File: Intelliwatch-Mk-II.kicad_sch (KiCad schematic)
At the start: 72 parts, among them J1 USB_C_Receptacle_USB2.0_16P, J101 DC Power Input, J2 CONN LCD 1.8 TFT SPI, J3 Conn 7S-4D HW-069 I2C, J4 Flashlight Terminals, J5 Voltmeter Probes, J6 DC Power Input, Q2 NDS331N, SW1 EN Button, SW2 PROG Button, SW3 Cherry MX Keyswitch, SW4 Cherry MX Keyswitch, SW5 Cherry MX Keyswitch, SW6 Cherry MX Keyswitch, SW7 LCD LED SPST, SW8 PWR SPST, SW9 PWR SPST, U1 LM7805, U10 SY8120IABC, U2 CH340C, U3 SN74HC02N, U4 LM1117T-3.3, U5 74AHC1G04GW_125, U6 74AHC1G04GW_125, U7 ESP32-WROOM-32UE, U8 QMC5883L, U9 MCP3421A0T-ECH

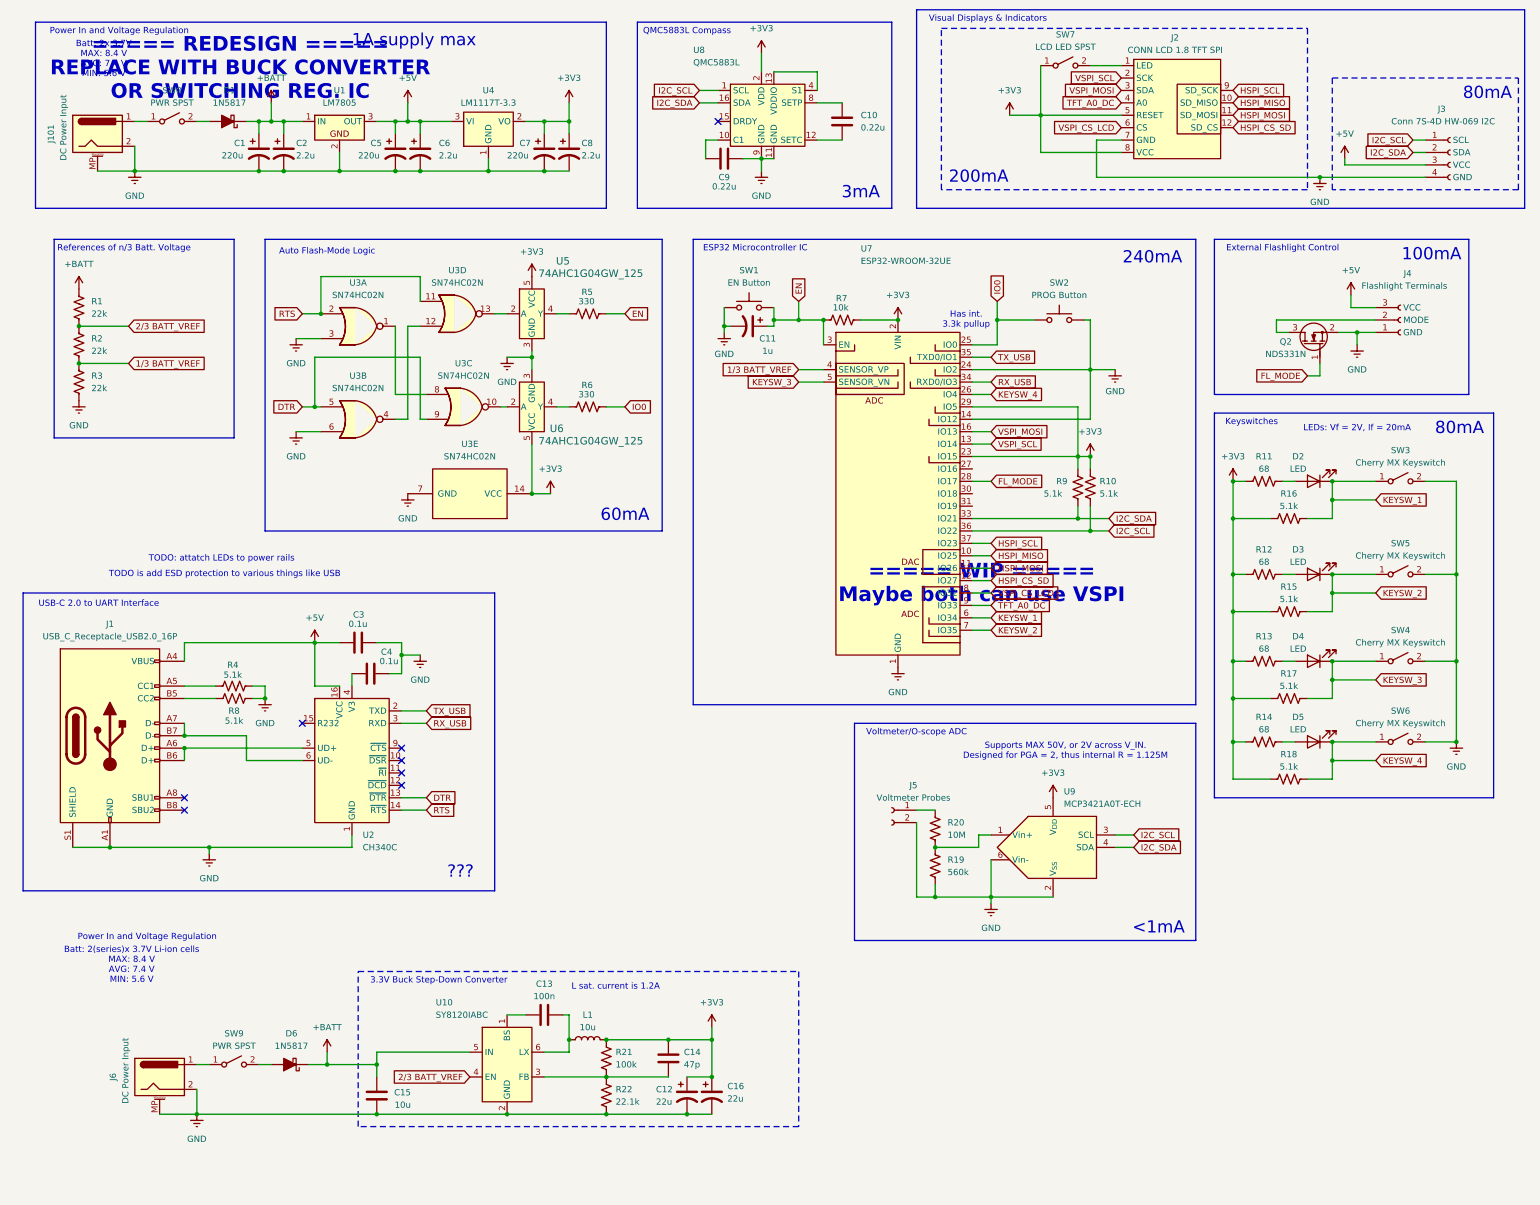
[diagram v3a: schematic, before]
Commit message: ADDED ESD protection diodes. FIXED power supply and voltage regulation. WIP figuring out if shared SPI bus is possible.
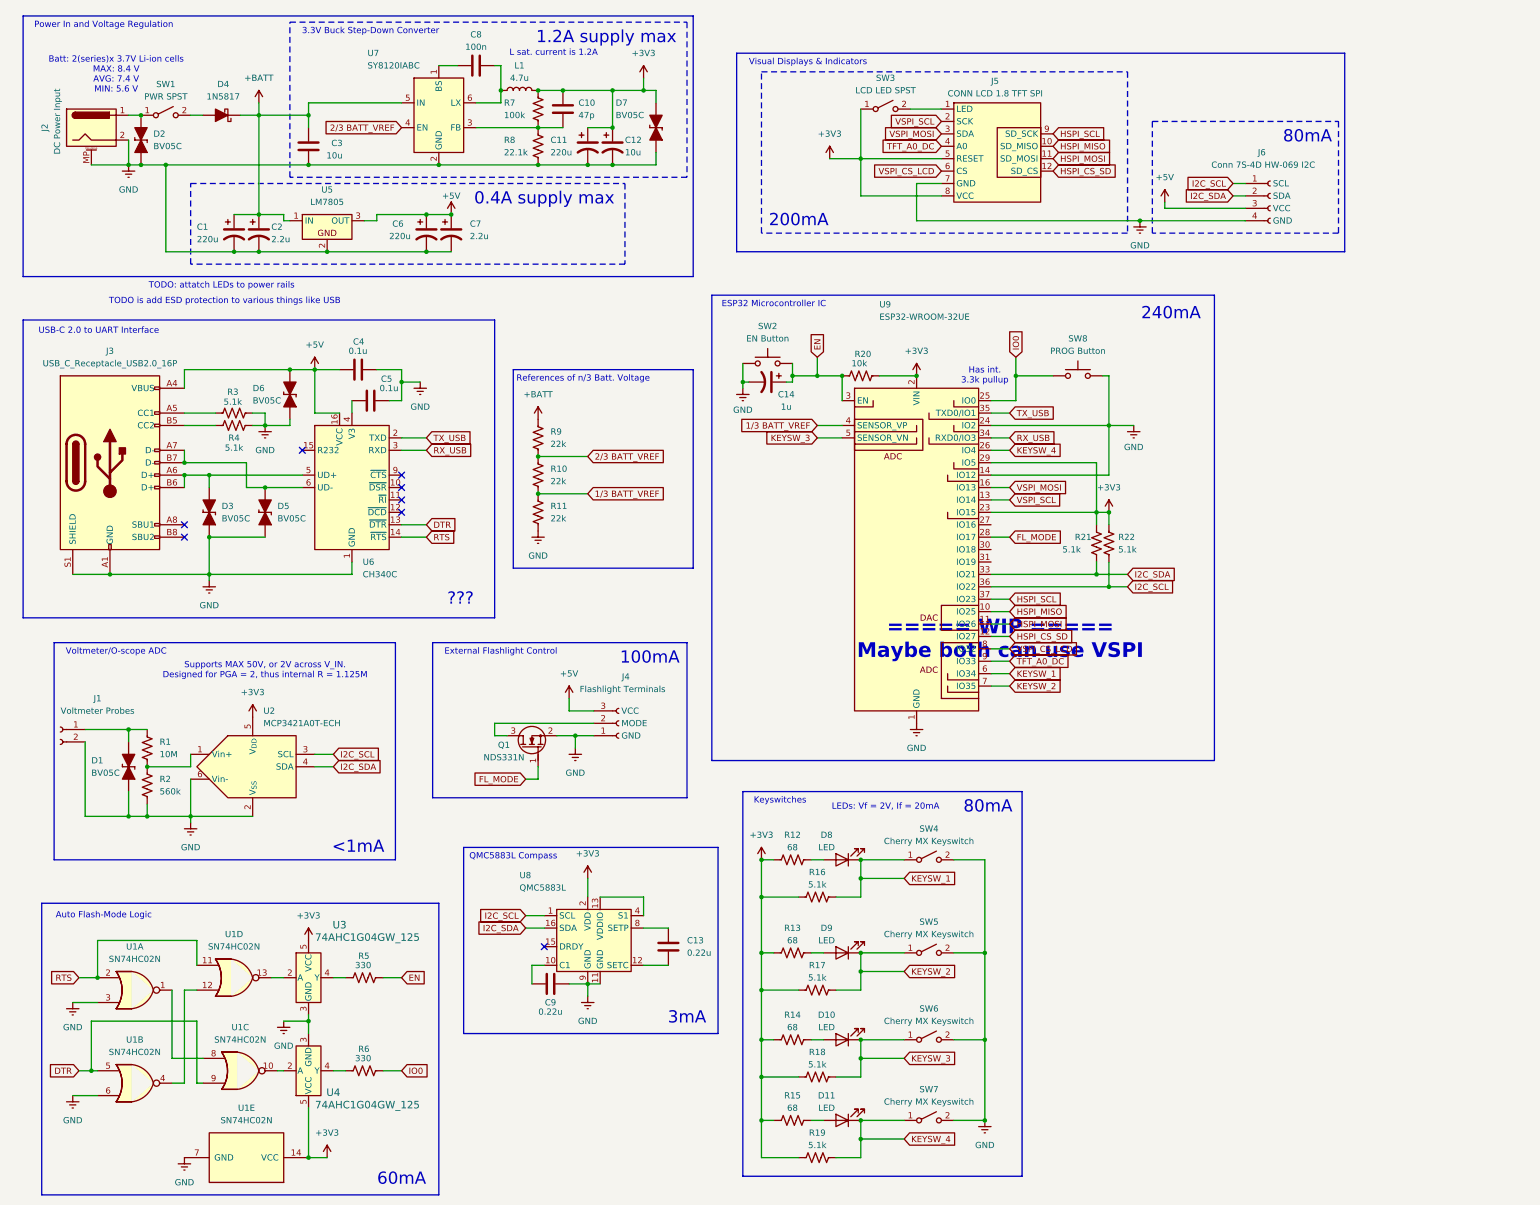
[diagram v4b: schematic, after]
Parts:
- removed C5: 220u, symbol Device:C_Polarized_US
- removed C8: 2.2u, symbol Device:C_Polarized_US
- removed D1: 1N5817, symbol Device:D_Schottky_Filled
- removed J101: DC Power Input, Connector_BarrelJack:BarrelJack_Horizontal, symbol Connector:Barrel_Jack_MountingPin
- removed SW8: PWR SPST, symbol Switch:SW_SPST
- removed U1: LM7805, PCM_Package_TO_SOT_THT_AKL:TO-220-3_Vertical, symbol PCM_Voltage_Regulator_AKL:LM7805CT
- removed U4: LM1117T-3.3, PCM_Package_TO_SOT_THT_AKL:TO-220-3_Vertical, symbol Regulator_Linear:LM1117T-3.3
- added D1, D2, D3, D5, D6, D7: BV05C, PCM_Diode_SMD_AKL:D_SOD-323_TVS, symbol PCM_Diode_TVS_AKL:D_TVS_Bidirectional_Generic
- added U5: LM7805, PCM_Package_TO_SOT_THT_AKL:TO-220-3_Vertical, symbol PCM_Voltage_Regulator_AKL:LM7805CT
- C11: renamed from C12; value 22u -> 220u
- C12: renamed from C16; value 22u -> 10u
- C6: value 2.2u -> 220u
- C7: value 220u -> 2.2u
- J1: renamed from J5; footprint (none) -> ZCustomFootprints:Standard IO Holes
- L1: value 10u -> 4.7u
- renumbered C14 to C10, C10 to C13, C11 to C14, C15 to C3, C3 to C4, C4 to C5, C13 to C8, D4 to D10, D5 to D11, D6 to D4, D2 to D8, D3 to D9, J6 to J2, J1 to J3, J2 to J5, J3 to J6, Q2 to Q1, R20 to R1, R2 to R10, R3 to R11, R11 to R12, R12 to R13, R13 to R14, R14 to R15, R15 to R17, R17 to R18, R18 to R19, R19 to R2, R7 to R20, R9 to R21, R10 to R22, R4 to R3, R8 to R4, R21 to R7, R22 to R8, R1 to R9, SW9 to SW1, SW1 to SW2, SW7 to SW3, SW3 to SW4, SW4 to SW6, SW6 to SW7, SW2 to SW8, U3 to U1, U9 to U2, U5 to U3, U6 to U4, U2 to U6, U10 to U7, U7 to U9
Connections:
- net +3V3: now also D7.1 (K); no longer C7.1
- net +5V: now also C7.1, D6.1 (K), U5.3 (OUT)
- net +BATT: now also U5.1 (IN)
- net GND: now also D1.2 (A), D2.2 (A), D3.2 (A), D5.2 (A), D6.2 (A), D7.2 (A), U5.2
- net at J2.1, SW1.1 (A): now also D2.1 (K)
- net at J1.1 (Pin_1), R1.2: now also D1.1 (K)
- net at J3.A6 (D+), J3.B6 (D+), U6.5 (UD+): now also D3.1 (K)
- net at J3.A7 (D-), J3.B7 (D-), U6.6 (UD-): now also D5.1 (K)
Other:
- note added: "0.4A supply max"
- note added: "1.2A supply max"
- note removed: "1A supply max"
- note removed: "===== REDESIGN ===== REPLACE WITH BUCK CONVERTER OR SWITCHING REG. IC"
- note removed: "Batt: 2x 3.7V MAX: 8.4 V AVG: 7.4 V MIN: 5.6 V"
- moved on the sheet: C10, C11, C12, C13, C14, C3, C4, C5, C8, C9, D10, D11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

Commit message: FIXED an ESD diode in the wrong place. ADDED Fluff. MODIFIED drawing sheet. REMOVED extra HSPI bus since SD and LCD can take turns using VSPI. ADDED LCSC Part # field for components.
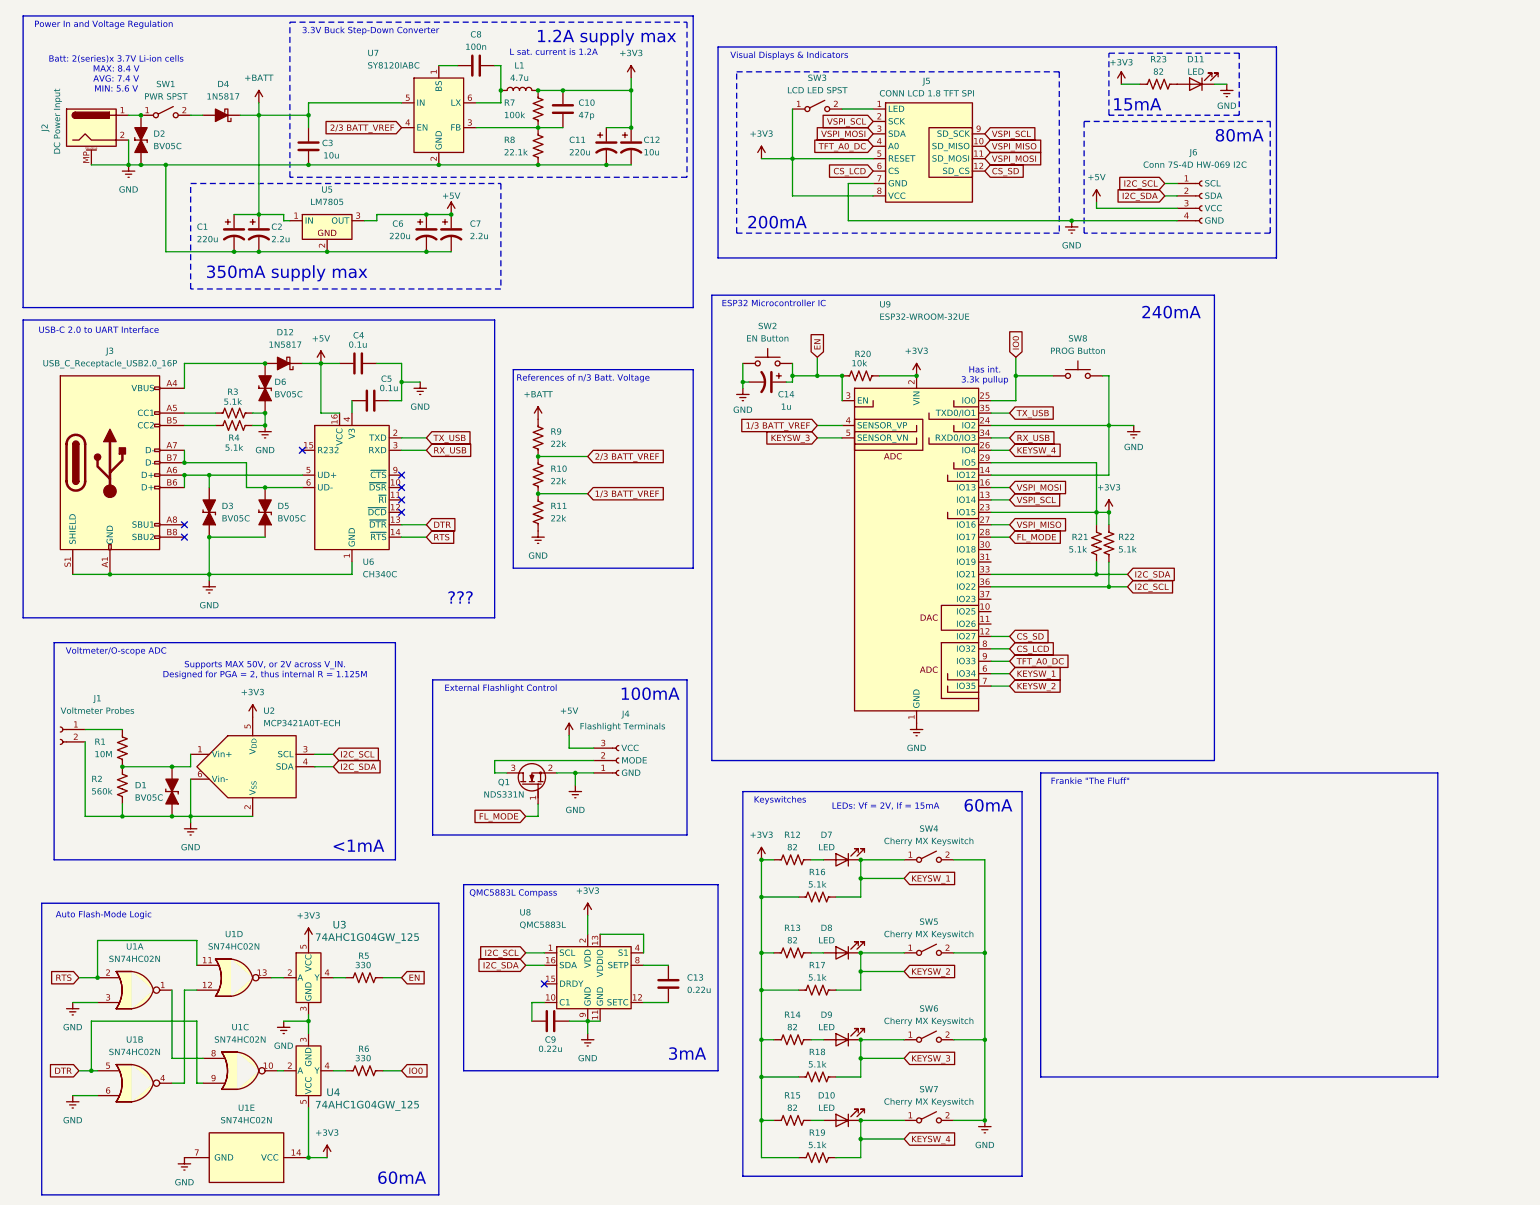
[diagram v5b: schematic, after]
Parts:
- removed D7: BV05C, PCM_Diode_SMD_AKL:D_SOD-323_TVS, symbol PCM_Diode_TVS_AKL:D_TVS_Bidirectional_Generic
- added D11: LED, LED_SMD:LED_0603_1608Metric, symbol Device:LED
- added D12: 1N5817, symbol Device:D_Schottky_Filled
- added R23: 82, symbol Device:R_US
- R12, R13, R14, R15: value 68 -> 82
- renumbered D11 to D10, D8 to D7, D9 to D8, D10 to D9
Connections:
- net +3V3: now also R23.1
- net +5V: now also D12.1 (K); no longer D6.1 (K), J3.A4 (VBUS), J3.A9 (VBUS), J3.B4 (VBUS), J3.B9 (VBUS)
- net GND: now also D11.1 (K)
- net VSPI_MOSI: now also J5.11 (SD_MOSI)
- net VSPI_SCL: now also J5.9 (SD_SCK)
- net at R1.1, R2.1, U2.1 (Vin+): now also D1.1 (K)
- net at J1.1 (Pin_1), R1.2: no longer D1.1 (K)
- net VSPI_MISO: now reaches U9.27 (IO16)
- net VSPI_MISO: now also J5.10 (SD_MISO)
- net HSPI_CS_SD renamed CS_SD
- net HSPI_MISO: no longer names the net of U9.10 (IO25)
- net HSPI_MISO: no longer J5.10 (SD_MISO)
- net HSPI_MOSI: no longer names the net of U9.11 (IO26)
- net HSPI_MOSI: no longer J5.11 (SD_MOSI)
- net HSPI_SCL: no longer names the net of U9.37 (IO23)
- net HSPI_SCL: no longer J5.9 (SD_SCK)
- net VSPI_CS_LCD renamed CS_LCD
- new net: D11.2 (A), R23.2
- new net: D12.2 (A), D6.1 (K), J3.A4 (VBUS), J3.A9 (VBUS), J3.B4 (VBUS), J3.B9 (VBUS)
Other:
- note added: "15mA"
- note added: "350mA supply max"
- note added: "Frankie "The Fluff""
- note added: "LEDs: Vf = 2V, If = 15mA"
- note removed: "0.4A supply max"
- note removed: "===== WIP ===== Maybe both can use VSPI"
- note removed: "LEDs: Vf = 2V, If = 20mA"
- note removed: "TODO is add ESD protection to various things like USB"
- note removed: "TODO: attatch LEDs to power rails"
- moved on the sheet: C11, C12, C13, C4, C9, D1, D6, J4, J5, J6, Q1, R1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

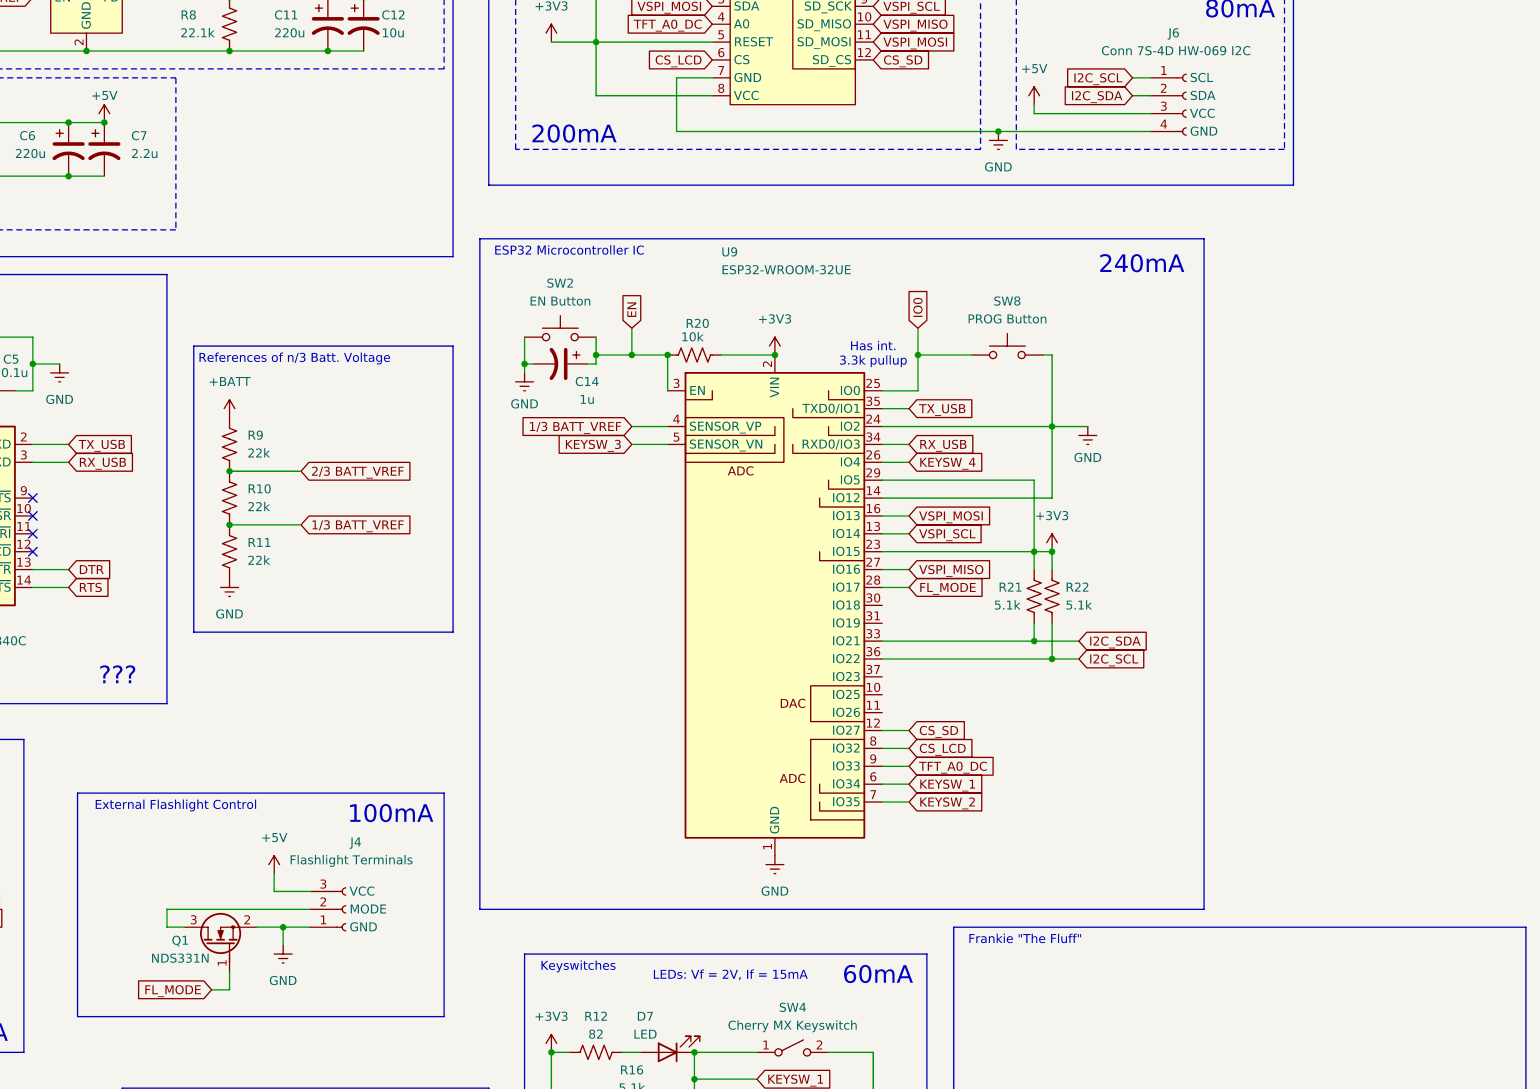
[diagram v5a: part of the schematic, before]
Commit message: WIP adding LCSC Part # fields to parts
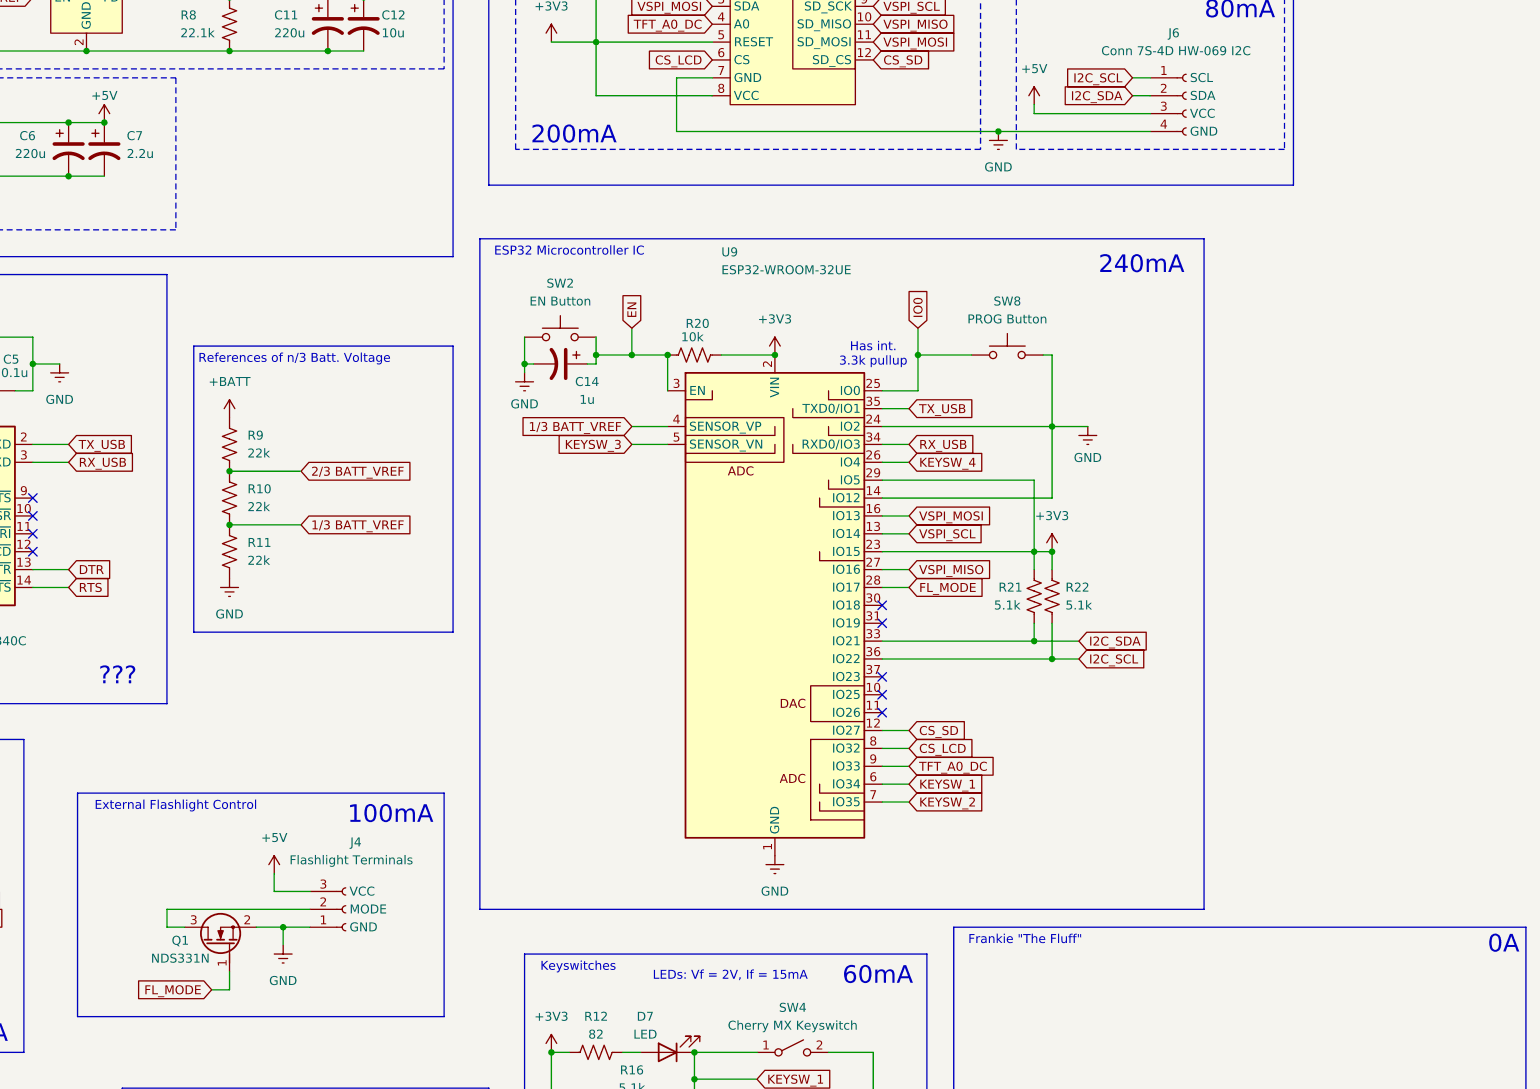
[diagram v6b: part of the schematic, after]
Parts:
- D1, D2, D3, D5, D6: LCSC Part # (none) -> C2841841
- D10, D11, D7, D8, D9: LCSC Part # (none) -> C497928
- D12, D4, J1, J2, J4, J5, J6, SW1, SW3, SW4, SW5, SW6, SW7: LCSC Part # (none) -> n/a
- J3: LCSC Part # (none) -> C2988369
- Q1: LCSC Part # (none) -> C192741
- SW2, SW8: LCSC Part # (none) -> C318938
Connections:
- no-connect marks 8 -> 13
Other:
- note added: "0A"
